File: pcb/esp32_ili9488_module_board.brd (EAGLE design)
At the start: 98 x 56.3 mm, 22 parts, among them U1 ILI9488 module, U2 ESP-WROOM/WROVER-32, U3 APK2112K-3.3TRG1, X1 HEADER-FTDI232, X2 USB-MICRO-B-FCI, X3 BOOT, X4 RESET, X5 QWIIC

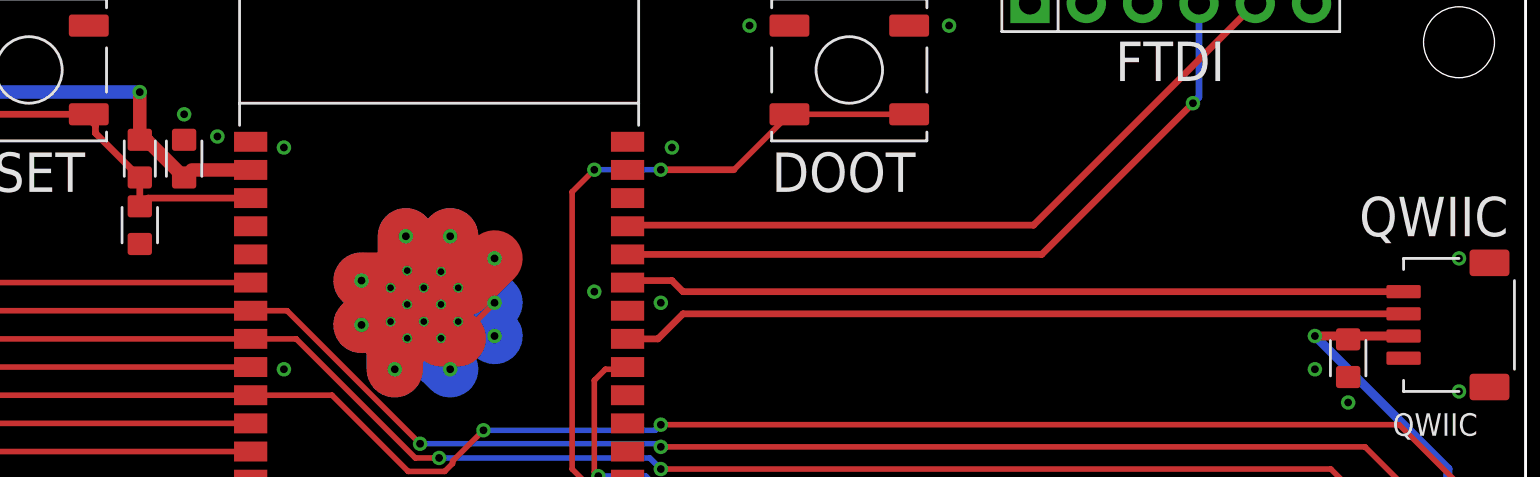
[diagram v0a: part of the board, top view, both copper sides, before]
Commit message: Add I2C pullups
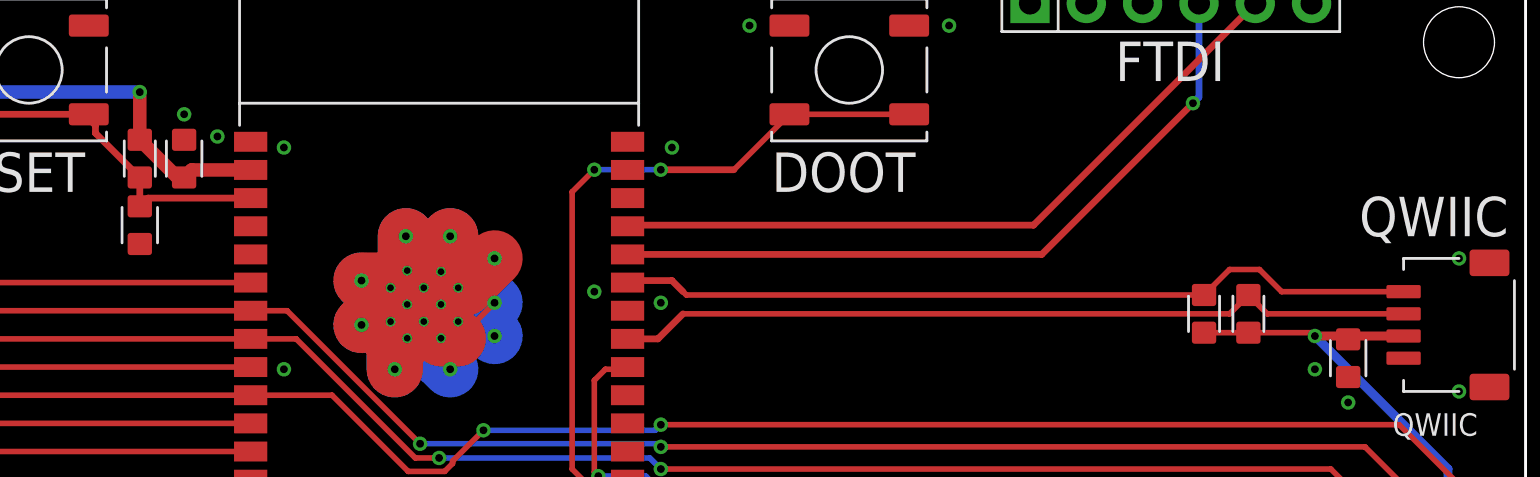
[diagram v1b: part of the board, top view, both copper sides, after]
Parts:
- added R1, R2: 10K, M2M-Passives:R0603
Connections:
- net 3.3V: now also R1.2, R2.2
- net SCL: now also R2.1
- net SDA: now also R1.1
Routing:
- net 3.3V: track 215.8 -> 221.3 mm
- net SCL: track 35.2 -> 36.2 mm
- net SDA: track 35.5 -> 36.2 mm
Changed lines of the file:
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@@
 <drawing>
 <settings>
-<setting alwaysvectorfont="yes"/>
+<setting alwaysvectorfont="no"/>
 <setting verticaltext="up"/>
 </settings>
@@
 <element name="U$1" library="M2M-Frames" package="BERGDAHL-20MM-TPLACE" value="" x="6.5" y="1" smashed="yes"/>
 <element name="U$2" library="M2M-Frames" package="OSHW-8MM-TPLACE" value="" x="14.5" y="13.5" smashed="yes"/>
+<element name="R1" library="M2M-Passives" package="R0603" value="10K" x="85.5" y="40.5" smashed="yes" rot="R270">
+<attribute name="NAME" x="86.4525" y="40.5" size="1.016" layer="25" rot="R270" align="bottom-center"/>
+<attribute name="NAME" x="85.5" y="40.5" size="0.6096" layer="51" rot="R270" align="center"/>
+<attribute name="VALUE" x="83.595" y="40.5" size="1.016" layer="27" rot="R270" align="bottom-center"/>
+</element>
+<element name="R2" library="M2M-Passives" package="R0603" value="10K" x="83.5" y="40.5" smashed="yes" rot="R270">
+<attribute name="NAME" x="84.4525" y="40.5" size="1.016" layer="25" rot="R270" align="bottom-center"/>
+<attribute name="NAME" x="83.5" y="40.5" size="0.6096" layer="51" rot="R270" align="center"/>
+<attribute name="VALUE" x="81.595" y="40.5" size="1.016" layer="27" rot="R270" align="bottom-center"/>
+</element>
 </elements>
 <signals>
@@
 <via x="35.5" y="50.5" extent="1-16" drill="0.35"/>
 <wire x1="35.5" y1="50.5" x2="11.5" y2="50.5" width="0.6096" layer="16"/>
-<wire x1="37.84" y1="46.99" x2="40.5" y2="46.99" width="0.6096" layer="1"/>
-<wire x1="37.5" y1="46.65" x2="35.8" y2="48.35" width="0.6096" layer="1"/>
-<wire x1="35.8" y1="48.35" x2="35.5" y2="48.35" width="0.6096" layer="1"/>
 <wire x1="80.8" y1="12.2" x2="80.8" y2="11.8" width="0.6096" layer="1"/>
 <wire x1="80.8" y1="11.8" x2="80.5" y2="11.5" width="0.6096" layer="1"/>
@@
 <wire x1="7" y1="11.5" x2="7" y2="46" width="0.6096" layer="16"/>
 <wire x1="7" y1="46" x2="11.5" y2="50.5" width="0.6096" layer="16"/>
-<wire x1="37.5" y1="46.65" x2="37.84" y2="46.99" width="0" layer="19" extent="1-1"/>
+<contactref element="R2" pad="2"/>
+<contactref element="R1" pad="2"/>
+<wire x1="83.5" y1="39.65" x2="85.5" y2="39.65" width="0.254" layer="1"/>
+<wire x1="85.5" y1="39.65" x2="88.35" y2="39.65" width="0.254" layer="1"/>
+<wire x1="88.35" y1="39.65" x2="88.5" y2="39.5" width="0.254" layer="1"/>
+<wire x1="40.5" y1="46.99" x2="37.84" y2="46.99" width="0.6096" layer="1"/>
+<wire x1="37.84" y1="46.99" x2="37.5" y2="46.65" width="0.6096" layer="1"/>
+<wire x1="35.5" y1="48.35" x2="37.2" y2="46.65" width="0.6096" layer="1"/>
+<wire x1="37.2" y1="46.65" x2="37.5" y2="46.65" width="0.6096" layer="1"/>
 </signal>
 <signal name="N$2">
@@
 <contactref element="X5" pad="SDA"/>
 <contactref element="U2" pad="31"/>
-<wire x1="92.5" y1="40.5" x2="60" y2="40.5" width="0.3048" layer="1"/>
 <wire x1="58.87" y1="39.37" x2="57.5" y2="39.37" width="0.3048" layer="1"/>
-<wire x1="60" y1="40.5" x2="58.87" y2="39.37" width="0.3048" layer="1"/>
+<wire x1="58.87" y1="39.37" x2="60" y2="40.5" width="0.3048" layer="1"/>
+<contactref element="R1" pad="1"/>
+<wire x1="84.65" y1="40.5" x2="85.5" y2="41.35" width="0.254" layer="1"/>
+<wire x1="60" y1="40.5" x2="84.65" y2="40.5" width="0.254" layer="1"/>
+<wire x1="92.5" y1="40.5" x2="86.35" y2="40.5" width="0.254" layer="1"/>
+<wire x1="86.35" y1="40.5" x2="85.5" y2="41.35" width="0.254" layer="1"/>
 </signal>
 <signal name="SCL">
 <contactref element="X5" pad="SCL"/>
 <contactref element="U2" pad="33"/>
-<wire x1="92.5" y1="41.5" x2="60" y2="41.5" width="0.3048" layer="1"/>
-<wire x1="60" y1="41.5" x2="59.5" y2="42" width="0.3048" layer="1"/>
+<wire x1="59.5" y1="42" x2="60" y2="41.5" width="0.3048" layer="1"/>
 <wire x1="59.5" y1="42" x2="57.59" y2="42" width="0.3048" layer="1"/>
 <wire x1="57.59" y1="42" x2="57.5" y2="41.91" width="0.3048" layer="1"/>
+<contactref element="R2" pad="1"/>
+<wire x1="60" y1="41.5" x2="60.15" y2="41.35" width="0.254" layer="1"/>
+<wire x1="60.15" y1="41.35" x2="83.5" y2="41.35" width="0.254" layer="1"/>
+<wire x1="83.5" y1="41.35" x2="84.65" y2="42.5" width="0.254" layer="1"/>
+<wire x1="86" y1="42.5" x2="87" y2="41.5" width="0.254" layer="1"/>
+<wire x1="87" y1="41.5" x2="92.5" y2="41.5" width="0.254" layer="1"/>
+<wire x1="84.65" y1="42.5" x2="86" y2="42.5" width="0.254" layer="1"/>
 </signal>
 </signals>
